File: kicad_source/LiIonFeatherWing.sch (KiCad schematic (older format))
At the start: 5 parts, among them CN1 ADAFRUIT_FEATHER, CN2 CONN_01X04, CN3 CONN_01X04, SW1 SWITCH_INV

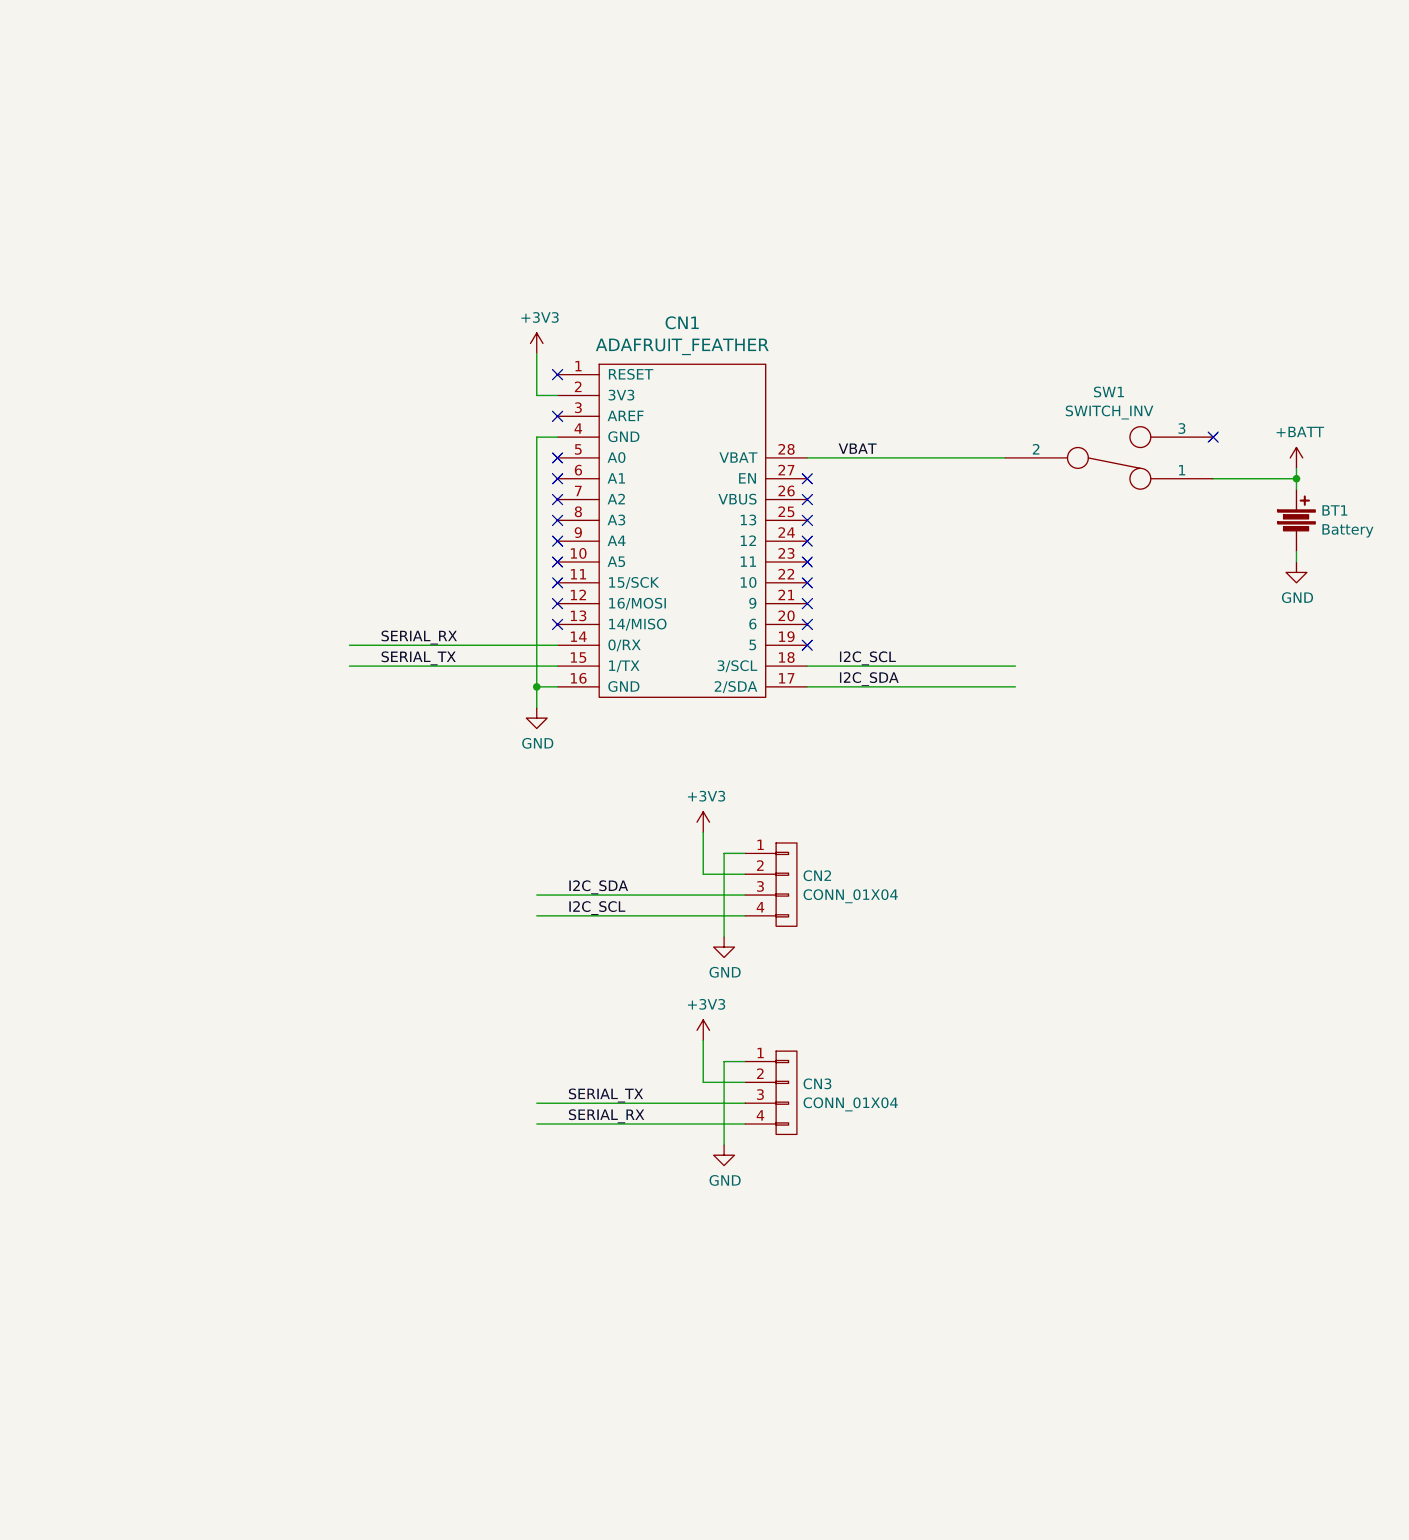
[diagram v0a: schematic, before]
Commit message: added mounting holes and labels
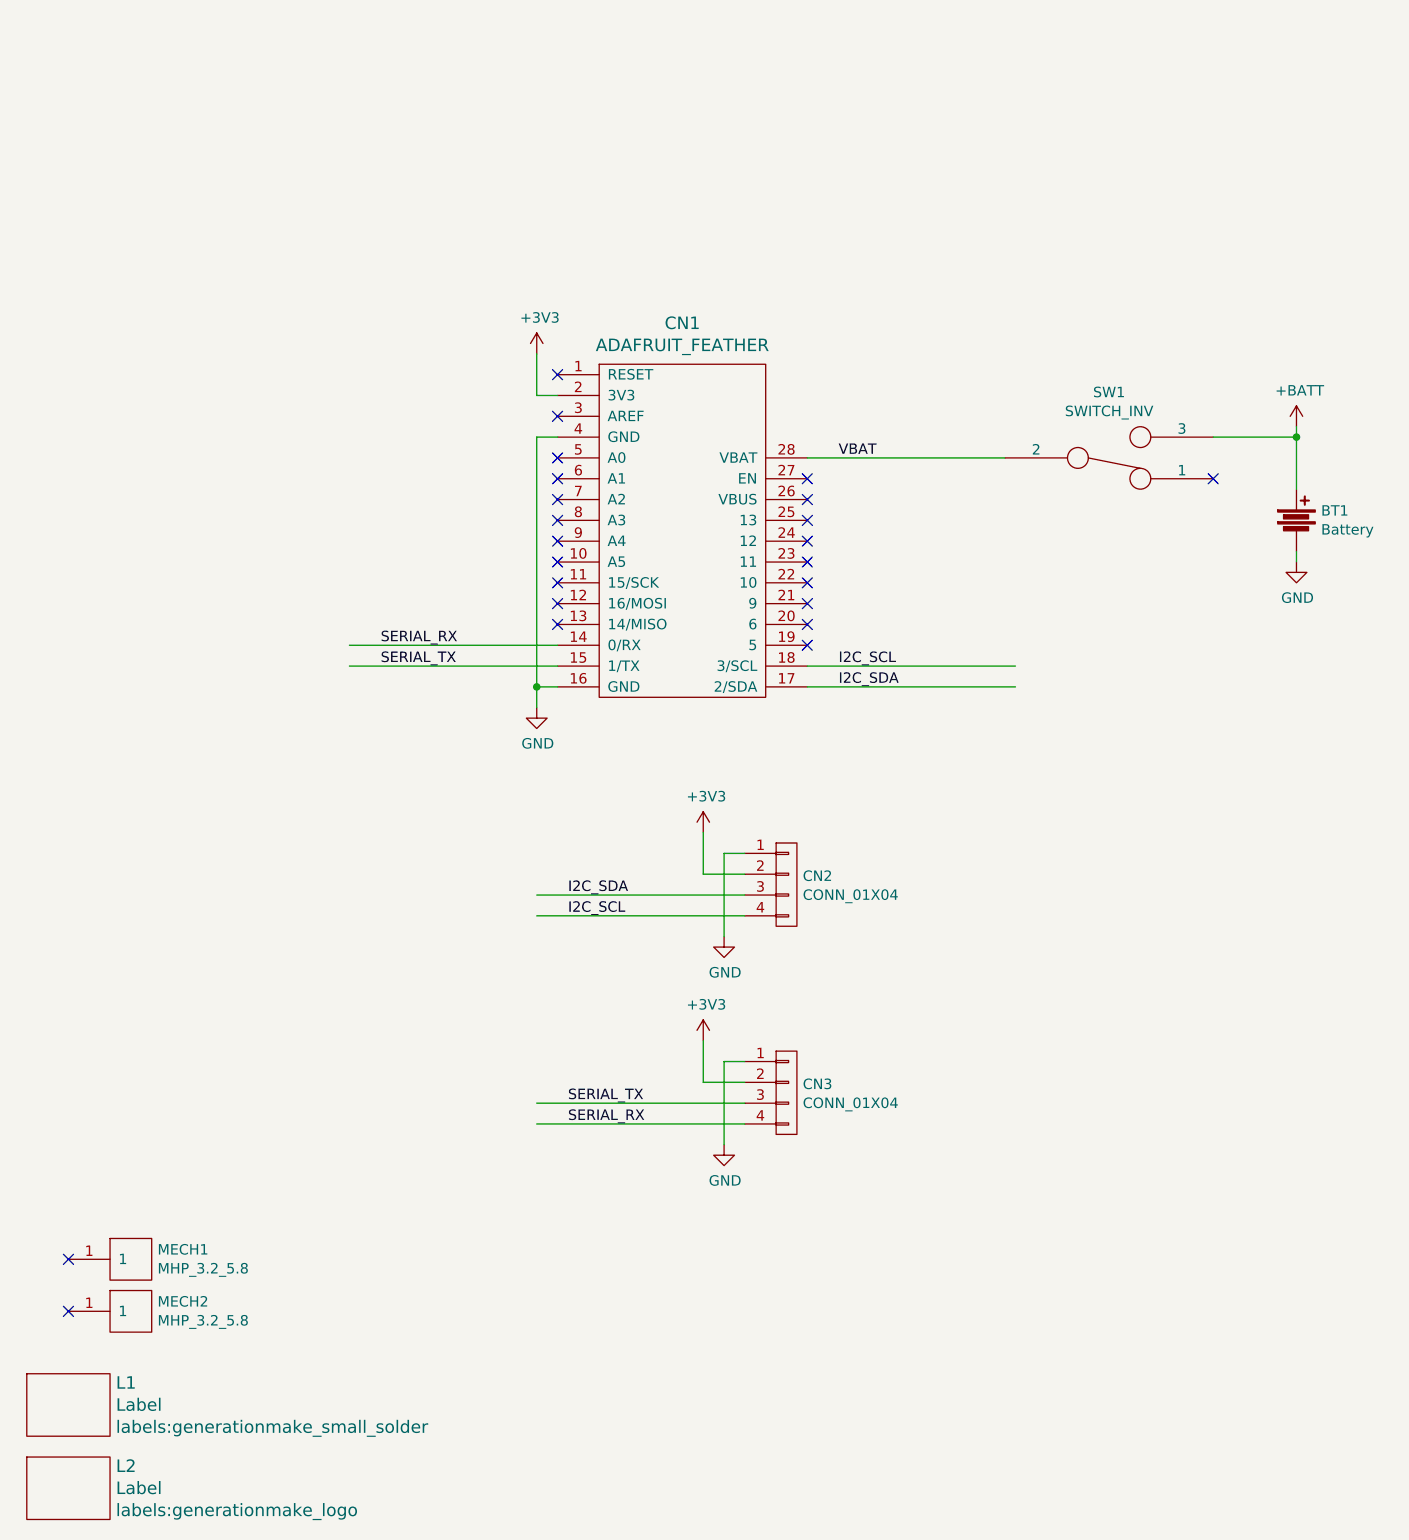
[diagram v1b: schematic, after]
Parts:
- added L1: Label, labels:generationmake_small_solder, symbol devices:Label
- added L2: Label, labels:generationmake_logo, symbol devices:Label
- added MECH1, MECH2: MHP_3.2_5.8, MECH_mounting_holes:MHP_3.2_5.8, symbol MECH_mounting-holes:MHP_3.2_5.8
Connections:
- no-connect marks 21 -> 23
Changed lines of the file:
@@
 L power-supply:+BATT #PWR07
 U 1 1 5F87A050
-P 6650 2650
-F 0 "#PWR07" H 6650 2500 50  0001 C CNN
-F 1 "+BATT" H 6665 2823 50  0000 C CNN
-F 2 "" H 6650 2650 50  0000 C CNN
-F 3 "" H 6650 2650 50  0000 C CNN
-	1    6650 2650
+P 6650 2450
+F 0 "#PWR07" H 6650 2300 50  0001 C CNN
+F 1 "+BATT" H 6665 2623 50  0000 C CNN
+F 2 "" H 6650 2450 50  0000 C CNN
+F 3 "" H 6650 2450 50  0000 C CNN
+	1    6650 2450
 	1    0    0    -1
 $EndComp
@@
 	1    0    0    1
 $EndComp
-NoConn ~ 6250 2500
 Wire Wire Line
 	5250 2600 4300 2600
 Wire Wire Line
-	6650 2650 6650 2700
-Wire Wire Line
 	6650 3050 6650 3100
-Wire Wire Line
-	6250 2700 6650 2700
-Connection ~ 6650 2700
-Wire Wire Line
-	6650 2700 6650 2750
 Wire Wire Line
 	3000 4800 4000 4800
@@
 NoConn ~ 4300 3400
 NoConn ~ 4300 3500
+Wire Wire Line
+	6650 2450 6650 2500
+Wire Wire Line
+	6250 2500 6650 2500
+Connection ~ 6650 2500
+Wire Wire Line
+	6650 2500 6650 2750
+NoConn ~ 6250 2700
+$Comp
+L devices:Label L2
+U 1 1 5F87C39C
+P 750 7550
+F 0 "L2" H 978 7656 60  0000 L CNN
+F 1 "Label" H 978 7550 60  0000 L CNN
+F 2 "labels:generationmake_logo" H 978 7444 60  0000 L CNN
+F 3 "" H 750 7550 60  0000 C CNN
+	1    750  7550
+	1    0    0    -1
+$EndComp
+$Comp
+L devices:Label L1
+U 1 1 5F87CDB9
+P 750 7150
+F 0 "L1" H 978 7256 60  0000 L CNN
+F 1 "Label" H 978 7150 60  0000 L CNN
+F 2 "labels:generationmake_small_solder" H 978 7044 60  0000 L CNN
+F 3 "" H 750 7150 60  0000 C CNN
+	1    750  7150
+	1    0    0    -1
+$EndComp
+$Comp
+L MECH_mounting-holes:MHP_3.2_5.8 MECH2
+U 1 1 5F87D203
+P 1050 6700
+F 0 "MECH2" H 1178 6746 50  0000 L CNN
+F 1 "MHP_3.2_5.8" H 1178 6655 50  0000 L CNN
+F 2 "MECH_mounting_holes:MHP_3.2_5.8" H 950 6750 50  0001 C CNN
+F 3 "" H 1050 6700 50  0001 C CNN
+	1    1050 6700
+	1    0    0    -1
+$EndComp
+NoConn ~ 750  6700
+$Comp
+L MECH_mounting-holes:MHP_3.2_5.8 MECH1
+U 1 1 5F87DA96
+P 1050 6450
+F 0 "MECH1" H 1178 6496 50  0000 L CNN
+F 1 "MHP_3.2_5.8" H 1178 6405 50  0000 L CNN
+F 2 "MECH_mounting_holes:MHP_3.2_5.8" H 950 6500 50  0001 C CNN
+F 3 "" H 1050 6450 50  0001 C CNN
+	1    1050 6450
+	1    0    0    -1
+$EndComp
+NoConn ~ 750  6450
 $EndSCHEMATC

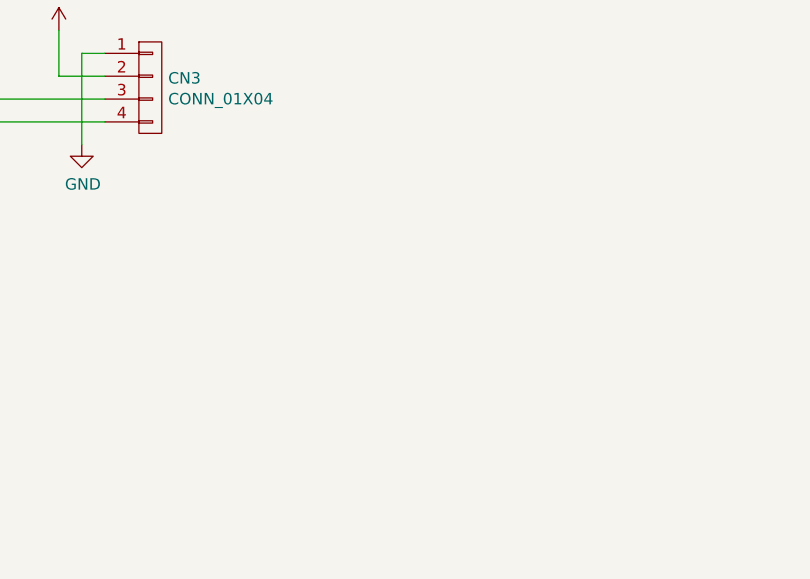
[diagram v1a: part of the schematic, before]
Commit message: added testpoints and array
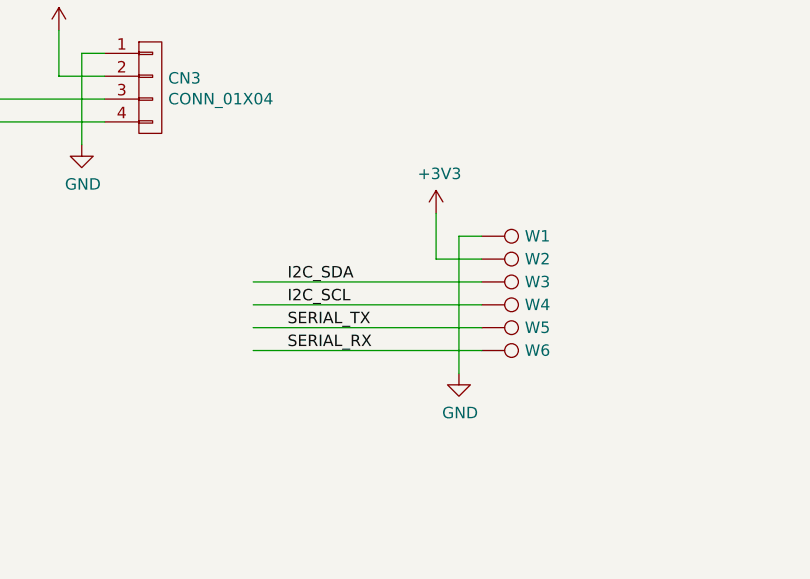
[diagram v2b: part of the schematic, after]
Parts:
- added W1, W2, W3, W4, W5, W6: TEST_1P, wire_pads:SolderWirePad_single_0-8mmDrill, symbol mechanical-connectors:TEST_1P
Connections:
- wire segments 27 -> 35
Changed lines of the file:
@@
 $EndComp
 NoConn ~ 750  6450
+Wire Wire Line
+	4650 6800 5650 6800
+Text Label 4800 6800 0    50   ~ 0
+SERIAL_RX
+Text Label 4800 6700 0    50   ~ 0
+SERIAL_TX
+Wire Wire Line
+	4650 6600 5650 6600
+Wire Wire Line
+	4650 6500 5650 6500
+Text Label 4800 6600 0    50   ~ 0
+I2C_SCL
+Text Label 4800 6500 0    50   ~ 0
+I2C_SDA
+$Comp
+L power-supply:+3V3 #PWR09
+U 1 1 5F88D918
+P 5450 6200
+F 0 "#PWR09" H 5450 6050 50  0001 C CNN
+F 1 "+3V3" H 5465 6373 50  0000 C CNN
+F 2 "" H 5450 6200 50  0000 C CNN
+F 3 "" H 5450 6200 50  0000 C CNN
+	1    5450 6200
+	1    0    0    -1
+$EndComp
+$Comp
+L power-supply:GND #PWR010
+U 1 1 5F88D922
+P 5550 6900
+F 0 "#PWR010" H 5550 6650 50  0001 C CNN
+F 1 "GND" H 5555 6727 50  0000 C CNN
+F 2 "" H 5550 6900 50  0000 C CNN
+F 3 "" H 5550 6900 50  0000 C CNN
+	1    5550 6900
+	1    0    0    -1
+$EndComp
+Wire Wire Line
+	5650 6300 5550 6300
+Wire Wire Line
+	5650 6400 5450 6400
+Wire Wire Line
+	5450 6400 5450 6200
+Wire Wire Line
+	4650 6700 5650 6700
+Wire Wire Line
+	5550 6300 5550 6900
+$Comp
+L mechanical-connectors:TEST_1P W1
+U 1 1 5F88F826
+P 5650 6300
+F 0 "W1" V 5650 6488 50  0000 L CNN
+F 1 "TEST_1P" V 5695 6488 50  0001 L CNN
+F 2 "wire_pads:SolderWirePad_single_0-8mmDrill" H 5850 6300 50  0001 C CNN
+F 3 "" H 5850 6300 50  0000 C CNN
+	1    5650 6300
+	0    1    1    0
+$EndComp
+$Comp
+L mechanical-connectors:TEST_1P W2
+U 1 1 5F88FE48
+P 5650 6400
+F 0 "W2" V 5650 6588 50  0000 L CNN
+F 1 "TEST_1P" V 5695 6588 50  0001 L CNN
+F 2 "wire_pads:SolderWirePad_single_0-8mmDrill" H 5850 6400 50  0001 C CNN
+F 3 "" H 5850 6400 50  0000 C CNN
+	1    5650 6400
+	0    1    1    0
+$EndComp
+$Comp
+L mechanical-connectors:TEST_1P W3
+U 1 1 5F88FF81
+P 5650 6500
+F 0 "W3" V 5650 6688 50  0000 L CNN
+F 1 "TEST_1P" V 5695 6688 50  0001 L CNN
+F 2 "wire_pads:SolderWirePad_single_0-8mmDrill" H 5850 6500 50  0001 C CNN
+F 3 "" H 5850 6500 50  0000 C CNN
+	1    5650 6500
+	0    1    1    0
+$EndComp
+$Comp
+L mechanical-connectors:TEST_1P W4
+U 1 1 5F89039D
+P 5650 6600
+F 0 "W4" V 5650 6788 50  0000 L CNN
+F 1 "TEST_1P" V 5695 6788 50  0001 L CNN
+F 2 "wire_pads:SolderWirePad_single_0-8mmDrill" H 5850 6600 50  0001 C CNN
+F 3 "" H 5850 6600 50  0000 C CNN
+	1    5650 6600
+	0    1    1    0
+$EndComp
+$Comp
+L mechanical-connectors:TEST_1P W5
+U 1 1 5F890700
+P 5650 6700
+F 0 "W5" V 5650 6888 50  0000 L CNN
+F 1 "TEST_1P" V 5695 6888 50  0001 L CNN
+F 2 "wire_pads:SolderWirePad_single_0-8mmDrill" H 5850 6700 50  0001 C CNN
+F 3 "" H 5850 6700 50  0000 C CNN
+	1    5650 6700
+	0    1    1    0
+$EndComp
+$Comp
+L mechanical-connectors:TEST_1P W6
+U 1 1 5F8908AE
+P 5650 6800
+F 0 "W6" V 5650 6988 50  0000 L CNN
+F 1 "TEST_1P" V 5695 6988 50  0001 L CNN
+F 2 "wire_pads:SolderWirePad_single_0-8mmDrill" H 5850 6800 50  0001 C CNN
+F 3 "" H 5850 6800 50  0000 C CNN
+	1    5650 6800
+	0    1    1    0
+$EndComp
 $EndSCHEMATC

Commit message: added schematic pdf, added images, updated project information
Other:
- note added: "find project information on\nhttps://github.com/generationmake/LiIonFeatherWing"
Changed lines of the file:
@@
 encoding utf-8
 Sheet 1 1
-Title ""
-Date ""
-Rev ""
-Comp ""
+Title "LiIonFeatherWing"
+Date "2020-10-15"
+Rev "0.1"
+Comp "generationmake"
 Comment1 ""
 Comment2 ""
@@
 	0    1    1    0
 $EndComp
+Text Notes 500  650  0    50   ~ 0
+find project information on\nhttps://github.com/generationmake/LiIonFeatherWing
 $EndSCHEMATC
